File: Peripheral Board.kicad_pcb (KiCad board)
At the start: 4 copper layers, 61.1 x 22.7 mm, 29 parts, among them J1 JAE_SIM_Card_SF72S006, J10 Conn_01x13_Male, J11 Conn_01x16_Male, J2 524372472, J4 5024268012, U1 MPU-9250, U7 XC6206-2.8V, U8 RT9166-12GVL

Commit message: add routing
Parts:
- C4, C48, C53, C54, C56, C57: moved to F.Cu
- moved C53 4.57 mm to (115.9, 57.2)
- moved C54 3.12 mm to (114.9, 54.5), turned to 90 degrees
- moved C48 3.05 mm to (114.9, 49.7), turned to 90 degrees
- moved C57 3.01 mm to (114.9, 52.6), turned to -90 degrees
- moved C56 2.54 mm to (114.9, 57.2)
- moved C4 2.00 mm to (112.3, 57.2)
- moved J2 0.99 mm to (115.8, 52.5)
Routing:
- net /CAM.PCLK: track 1.96 -> 6.30 mm, vias 0 -> 1
- net GND: track 8.31 -> 4.33 mm
- net /CAM.SDA: track 9.38 -> 5.60 mm
- net +2V8: track 9.77 -> 7.61 mm, vias 1 -> 2
- net +3V3: track 12.3 -> 13.9 mm, vias 5 -> 7
- net +1V2: track 10.5 -> 9.91 mm
- net +1V8: track 1.99 -> 1.63 mm, vias 0 -> 1

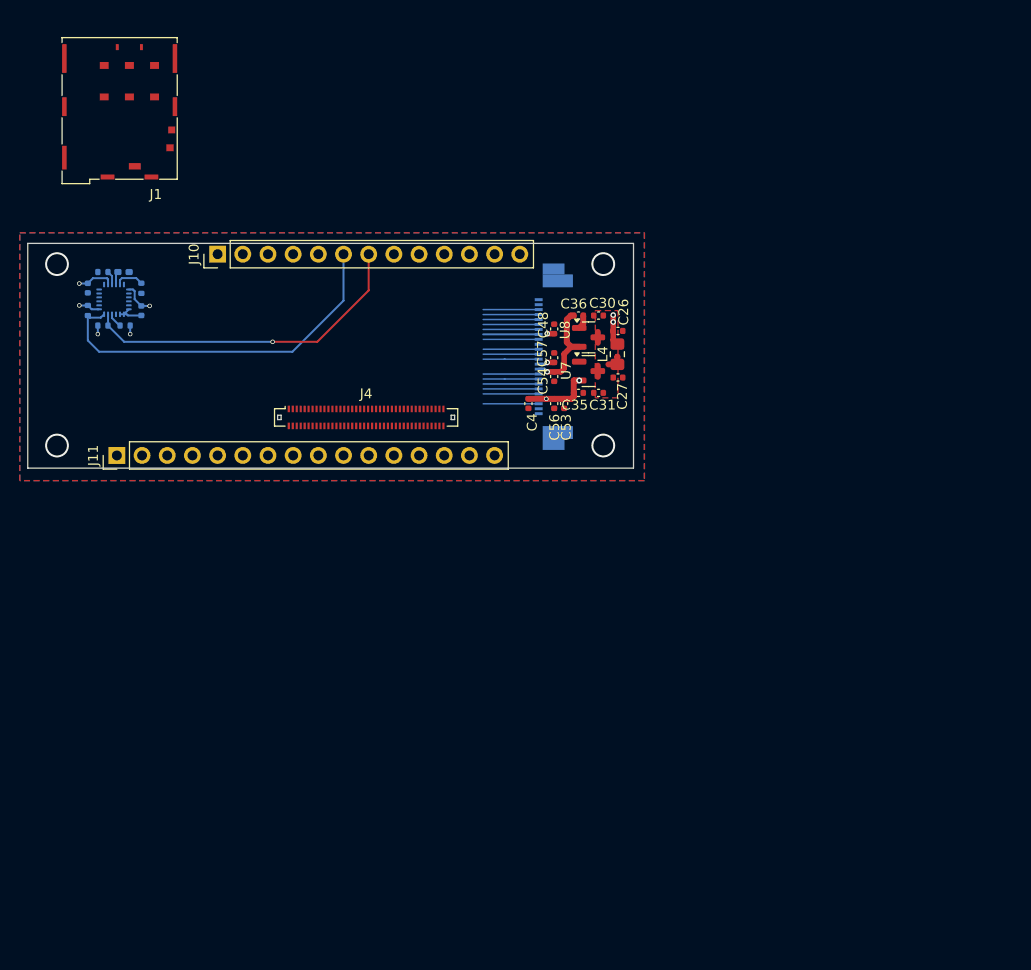
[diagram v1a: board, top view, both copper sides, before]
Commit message: Added sd card, routed camera, and added esp32c3
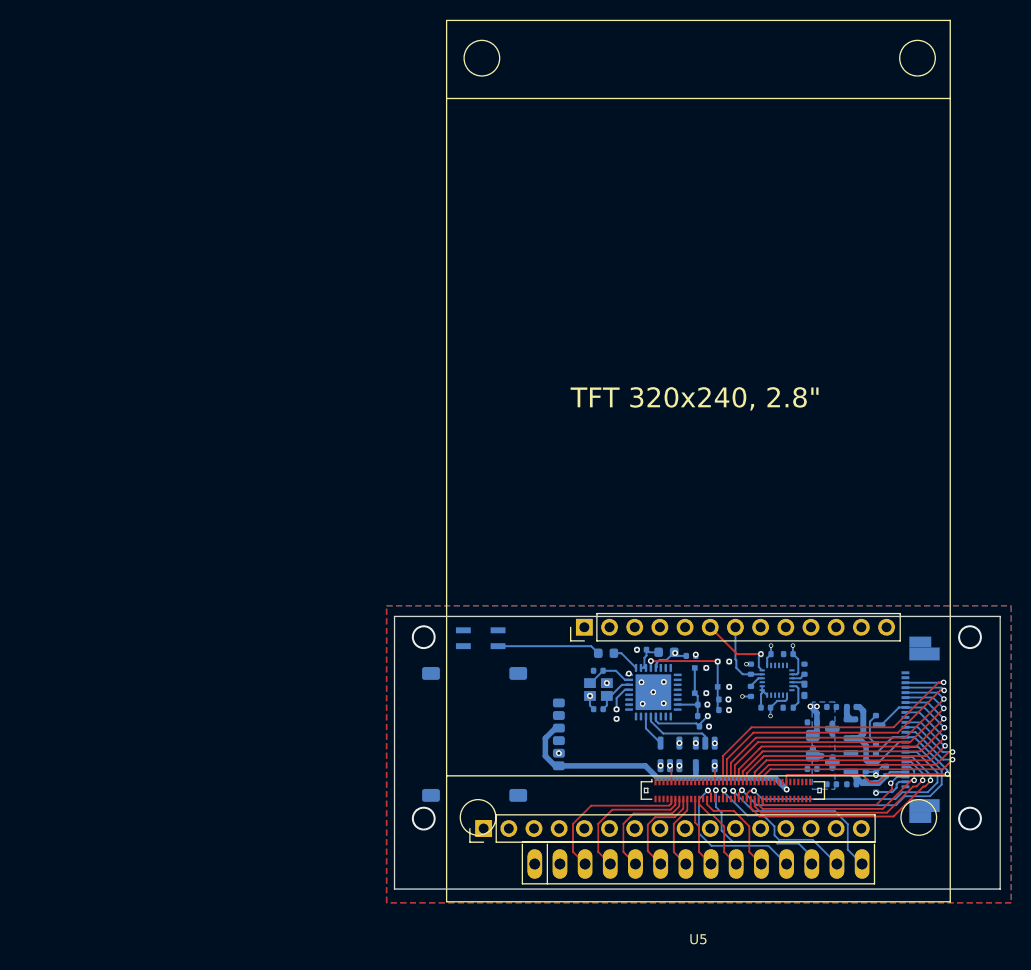
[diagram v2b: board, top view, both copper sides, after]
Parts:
- removed J1: JAE_SIM_Card_SF72S006, Connector_JAE:JAE_SIM_Card_SF72S006
- added ANT1: 2450AT42E0100E, footprints:2450AT42E0100E-ANT, B.Cu at (107.5, 80.9)
- added C18: 10uF, Capacitor_SMD:C_0402_1005Metric, B.Cu at (130.0, 89.8)
- added C19: 1uF, Capacitor_SMD:C_0402_1005Metric, B.Cu at (121.2, 88.6)
- added C20: 0.1uF, Capacitor_SMD:C_0402_1005Metric, B.Cu at (128.7, 82.7)
- added C21: 0.1uF, Capacitor_SMD:C_0402_1005Metric, B.Cu at (123.7, 82.1)
- added C23: 22pF, Capacitor_SMD:C_0402_1005Metric, B.Cu at (129.9, 87.6)
- added C5: 22pF, Capacitor_SMD:C_0402_1005Metric, B.Cu at (119.4, 84.2)
- added C6: 22pF, Capacitor_SMD:C_0402_1005Metric, B.Cu at (119.4, 88.1)
- added C7: 1uF, Capacitor_SMD:C_0402_1005Metric, B.Cu at (132.0, 87.1)
- added J3: SIM_Card, Connector_Card:nanoSIM_GCT_SIM8060-6-0-14-00, B.Cu at (108.6, 90.6)
- added L1: L, Inductor_SMD:L_0603_1608Metric, B.Cu at (120.1, 82.4)
- added L5: L, Inductor_SMD:L_0603_1608Metric, B.Cu at (126.2, 82.3)
- added R18: 10k, Resistor_SMD:R_0402_1005Metric, B.Cu at (129.9, 88.8)
- added R2: 10k, Resistor_SMD:R_0402_1005Metric, B.Cu at (132.0, 88.1)
- added SW1: SW_Push_Dual, footprints:switch_SKSVCCE010, B.Cu at (132.0, 84.5)
- added SW2: SW_Push_Dual, footprints:switch_SKSVCCE010, B.Cu at (129.7, 85.2)
- added U2: ESP32-C6FH4, Package_DFN_QFN:QFN-32-1EP_5x5mm_P0.5mm_EP3.6x3.6mm, B.Cu at (124.9, 86.3)
- added U3: SN74LV1T125DBV, Package_TO_SOT_SMD:SOT-23-5, B.Cu at (130.1, 92.6)
- added U4: SN74LV1T125DBV, Package_TO_SOT_SMD:SOT-23-5, B.Cu at (126.6, 92.6)
- added U5: TFT_320x240, Library:TFT-320x240, F.Cu at (129.4, 103.7)
- added X1: Crystal 40 Mhz 10ppm, footprints:Crystal_ECS-40Mhz_ECS, B.Cu at (119.4, 86.1)
- C26, C27, C30, C31, C35, C36, C4, C48, C53, C54, C56, C57, L4, U7, U8: moved to B.Cu
- moved R17 81.3 mm to (140.1, 84.0), turned to 90 degrees
- moved C1 80.6 mm to (140.1, 86.1), turned to -90 degrees
- moved C3 79.7 mm to (138.5, 82.5), turned to 180 degrees
- moved R16 77.8 mm to (138.5, 87.9), turned to 180 degrees
- moved U1 77.1 mm to (137.4, 85.1), turned to -90 degrees
- moved R10 76.7 mm to (136.3, 82.5), turned to 180 degrees
- moved C2 74.6 mm to (136.2, 87.9), turned to 180 degrees
- moved R11 74.0 mm to (134.7, 84.0), turned to -90 degrees
- moved R15 73.1 mm to (134.7, 86.3), turned to 90 degrees
- moved J2 52.8 mm to (152.8, 90.1)
- moved J10 52.8 mm to (117.9, 79.8)
- moved J4 52.8 mm to (132.9, 96.3)
- moved J11 52.8 mm to (107.8, 100.1)
- moved C4 51.7 mm to (148.4, 94.3), turned to -90 degrees
- moved C57 51.1 mm to (147.4, 92.1)
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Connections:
- J4 pad 26: VCC_BANK34 -> unconnected-(J4-Pin_26-Pad26)
- J4 pad 35: /FPGA_T15 -> /CAM.D4
- J4 pad 37: /FPGA_U14 -> /CAM.D3
- J4 pad 39: /FPGA_T14 -> /CAM.D5
- J4 pad 40: VCC_BANK34 -> unconnected-(J4-Pin_40-Pad40)
- J4 pad 41: /FPGA_U13 -> /CAM.D2
- J4 pad 43: /FPGA_R14 -> /CAM.D6
- J4 pad 44: /FPGA_V13 -> /CAM.HREF
- J4 pad 45: /FPGA_U12 -> /CAM.PCLK
- J4 pad 47: /FPGA_T12 -> /CAM.D7
- J4 pad 48: /FPGA_V12 -> /CAM.PWDN
- J4 pad 50: /FPGA_W11 -> /CAM.VSYNC
- J4 pad 51: /FPGA_T11 -> /CAM.D8
- J4 pad 52: /FPGA_V11 -> /CAM.RST
- J4 pad 53: /FPGA_U10 -> /CAM.MCLK
- J4 pad 54: /FPGA_W10 -> /CAM.SCL
- J4 pad 55: /FPGA_T10 -> /CAM.D9
- J4 pad 56: /FPGA_V10 -> /CAM.SDA
- J4 pad 58: VCC_BANK34 -> unconnected-(J4-Pin_58-Pad58)
- J4 pad 64: /ARD_AREF -> unconnected-(J4-Pin_64-Pad64)
- J4 pad 66: VCC_BANK34 -> unconnected-(J4-Pin_66-Pad66)
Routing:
- net +1V8: track 1.63 -> 58.6 mm, vias 1 -> 2
- net /PS_MIO11_SDA: track 37.5 -> 8.10 mm, vias 0 -> 1
- net /PS_MIO10_SCL: track 33.9 -> 7.02 mm, vias 1 -> 0
- net /CAM.D4: track 5.60 -> 31.8 mm, vias 0 -> 1
- net /CAM.PCLK: track 6.30 -> 31.8 mm
- net /CAM.D3: track 5.60 -> 31.1 mm, vias 0 -> 1
- net /CAM.D5: track 5.60 -> 30.2 mm, vias 0 -> 1
- net /CAM.D2: track 5.60 -> 29.5 mm, vias 0 -> 1
- net /CAM.HREF: track 5.60 -> 28.7 mm, vias 0 -> 1
- net /CAM.D6: track 5.60 -> 28.6 mm, vias 0 -> 1
- net /CAM.D7: track 5.60 -> 27.3 mm, vias 0 -> 1
- net /CAM.MCLK: track 5.60 -> 27.0 mm, vias 0 -> 1
- net /CAM.D8: track 5.60 -> 26.3 mm, vias 0 -> 1
- net /CAM.D9: track 5.61 -> 26.3 mm, vias 0 -> 1
- net /CAM.PWDN: track 5.60 -> 26.0 mm, vias 0 -> 1
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- added copper zone on B.Cu, net /pwr
- removed copper zone on F.Cu, net /pwr
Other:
- board size 61.1 x 22.7 mm -> 61.1 x 27.5 mm
